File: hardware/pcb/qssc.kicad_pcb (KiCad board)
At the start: 6 copper layers, 210 x 140 mm, 126 parts, among them J1 FT232RL, J10 USB-C, J12 BTB_HOST, J2 5V Barrel, J3 SMA, J4 12V LED, J7 RESET, J8 MW_GATE, J9 JTAG, U1 XC7A35T-1CSG324C, U3 ADF4351BCPZ, U5 GVA-84+, U8 W25Q128JVSIQ, Y1 100MHz TCXO

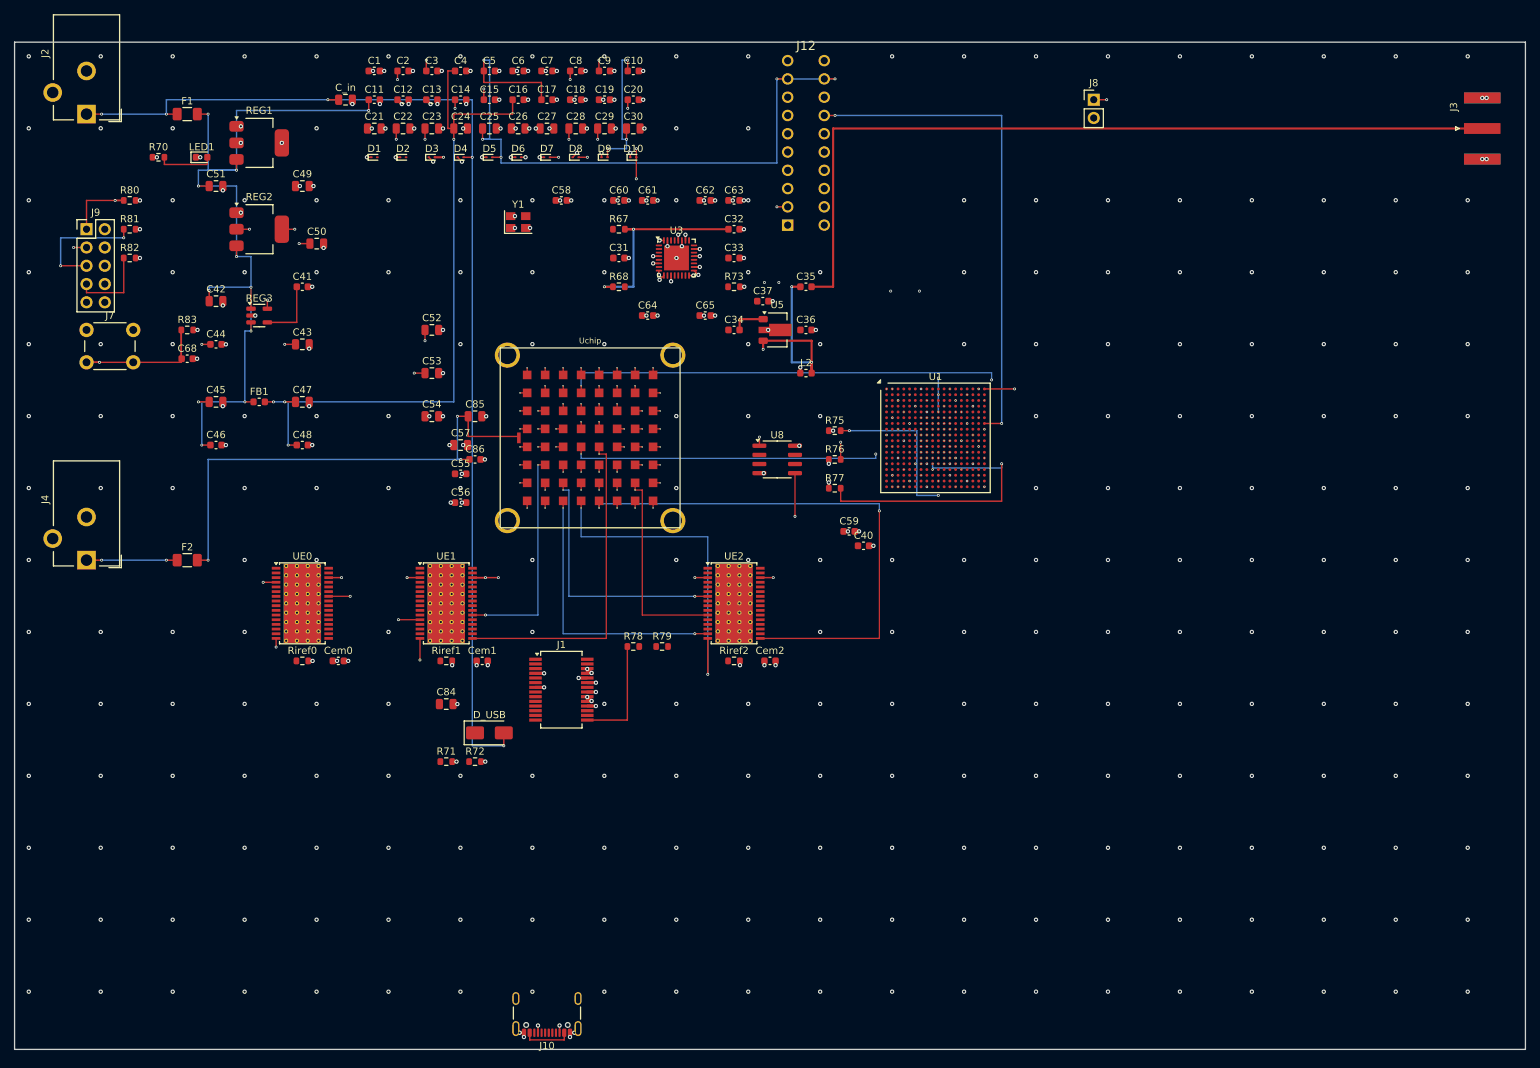
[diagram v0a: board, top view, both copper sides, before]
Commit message: head: bump detector head to 6 layers (4 signal layers for the die bus)
The 4-layer head put the 64-net die bus (DET_IN + DET_TIA) on only 2 signal
layers (F.Cu/B.Cu), at the autorouter's density ceiling.  6 layers add
In3.Cu + In4.Cu signal layers so route_signals + FreeRouting have 4 signal
layers (F.Cu/In3.Cu/In4.Cu/B.Cu).  route_signals.build() auto-selects the
4-signal-layer set from GetCopperLayerCount() (>4 branch), no router edit
needed; route_qssc_pcb reads plane labels dynamically.  HEAD_STACK_UP is a
6-layer 1.6mm FR4 build (In1.Cu GND one 0.15mm prepreg below F.Cu for the
TIA->ADC analog reference).  Die Uchip 64 DET pads stay on B.Cu.

Main board (qssc.*) is regenerated too: the JTAG J9 pin-9 +3V3 (VREF) fix
now comes from the generator code (replacing the earlier surgical edit),
and the .kicad_pcb is re-serialised in generator format (cosmetic
normalisation -- no layout/net change).  ruff CI rule clean.

Co-Authored-By: Claude Code <noreply@anthropic.com>
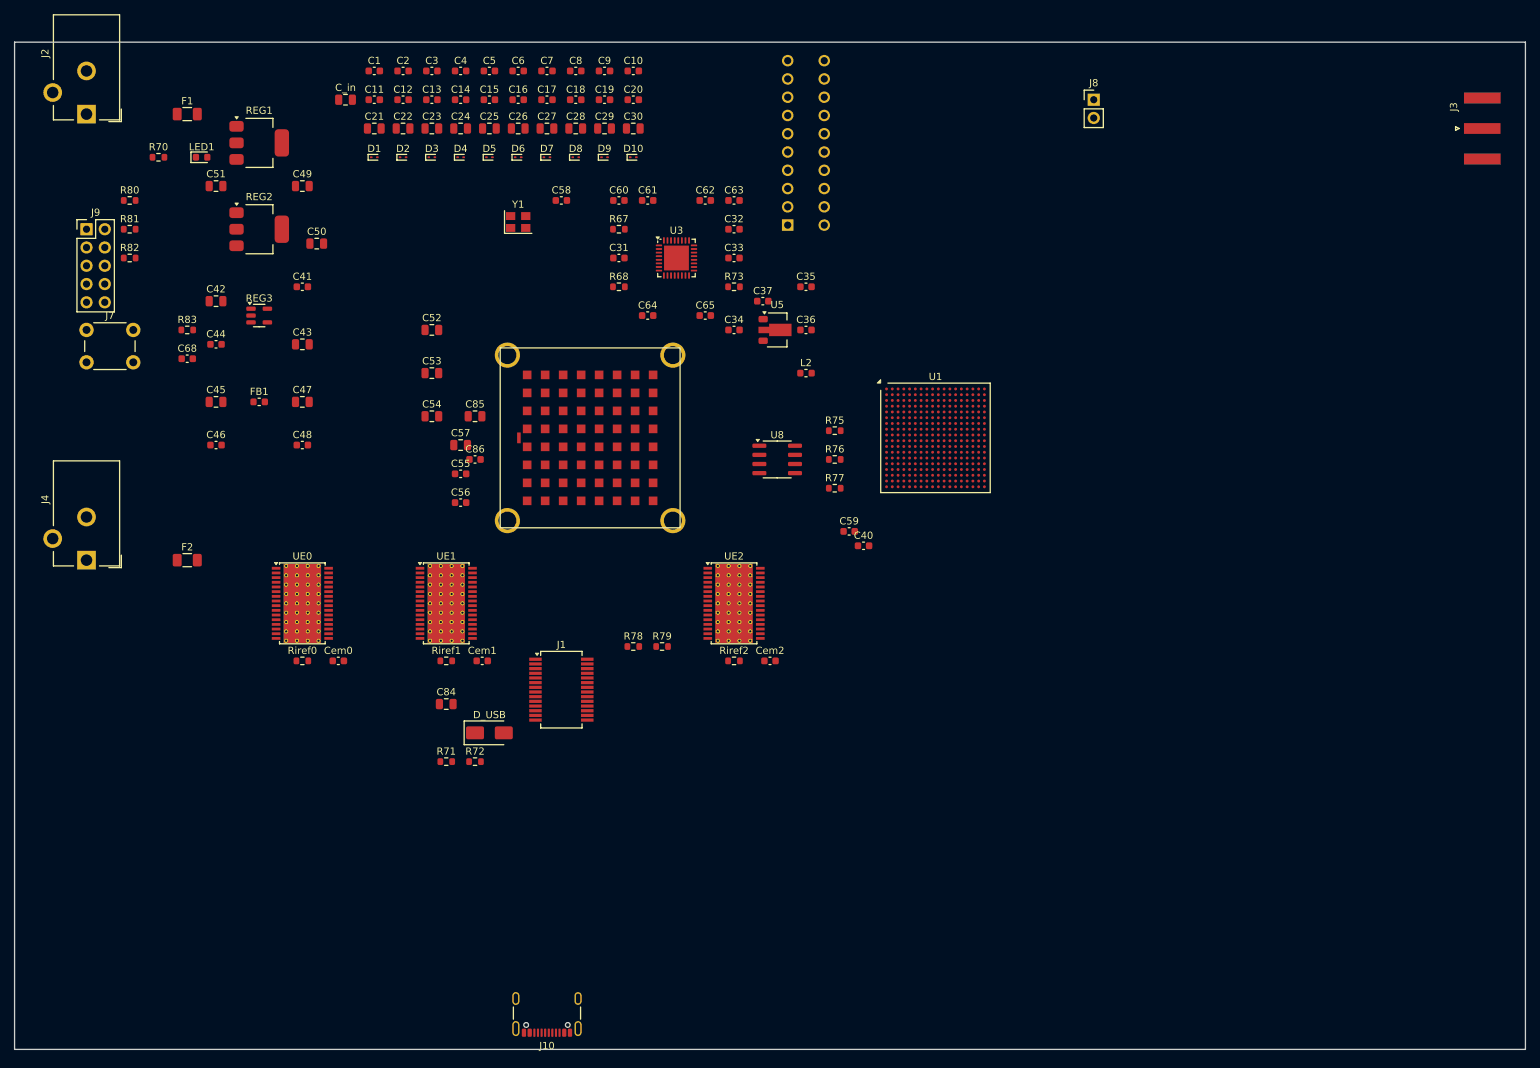
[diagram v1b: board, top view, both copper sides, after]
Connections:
- U3 pad : (no net) -> GND
- UE0 pad : (no net) -> GND
- UE1 pad : (no net) -> GND
- UE2 pad : (no net) -> GND
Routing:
- net +1V0: track 255.6 -> 0.00 mm, vias 27 -> 0
- net +5V: track 216.3 -> 0.00 mm, vias 16 -> 0
- net emitter_cat11: track 198.6 -> 0.00 mm, vias 3 -> 0
- net +1V8: track 157.6 -> 0.00 mm, vias 16 -> 0
- net +5V_IN: track 155.8 -> 0.00 mm, vias 5 -> 0
- net TCK: track 154.6 -> 0.00 mm, vias 3 -> 0
- net mw_gate: track 151.8 -> 0.00 mm, vias 5 -> 0
- net emitter_cat35: track 147.7 -> 0.00 mm, vias 3 -> 0
- net TDO: track 147.3 -> 0.00 mm, vias 2 -> 0
- net reset: track 138.6 -> 0.00 mm, vias 2 -> 0
- net em_xlat: track 137.1 -> 0.00 mm, vias 5 -> 0
- net em_sclk: track 122.2 -> 0.00 mm, vias 2 -> 0
- net +5V_RF: track 116.7 -> 0.00 mm, vias 8 -> 0
- net J3_SIG: track 115.2 -> 0.00 mm
- net em_sin: track 102.5 -> 0.00 mm, vias 2 -> 0
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- removed copper zone on In2.Cu, net +3V3
- removed copper zone on In1.Cu, net GND

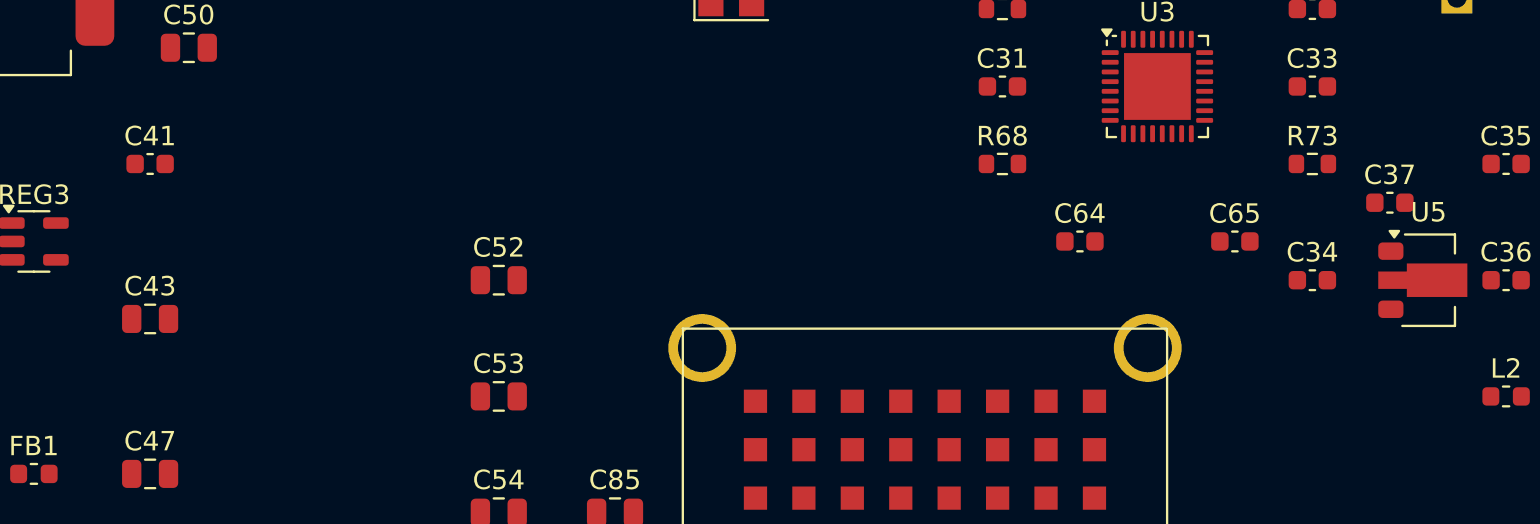
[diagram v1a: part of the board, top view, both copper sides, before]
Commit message: pins: per-datasheet fixes (ADF4351 VCOM, FT232 CBUS0/NC, AP2127K pin4) + FPGA clock on P-side MRCC
Per-datasheet verification of all 11 components (real PDFs / KiCad symbols /
manufacturer datasheets) found 4 confirmed pin defects, now fixed:

- ADF4351 pin 23 (VCOM, internal compensation node biased at half the tuning
  range) was tied direct to GND -- shorting the half-range bias. Now decoupled
  to GND via a 100nF cap on a dedicated ADF_VCOM net (mirrors VREF/C36 and
  TEMP/C37). Verified from ADF4351.pdf p8 Pin Function table.
- FT232RL pin 23 is CBUS0 (not AGND); pin 24 is NC (not a 2nd VCC pad). The
  prior 'fix' tied 23->GND and 24->+3V3 under a wrong pin belief. Now both are
  no_connect; the real AGND is pin 25 (already GND). TXD/RXD comment labels
  corrected (nets are named from the FPGA side); 3V3OUT decoupler is C55 not C57.
  Verified from the KiCad Interface_USB:FT232RL symbol (omits NC pads 8 & 24).
- AP2127K-1.0 (REG3) fixed-output pin 4 is NC, not BP -- the prior C41 10nF
  tied a cap to a floating NC pad. Pin 4 -> no_connect; C41 designator reused
  for the ADF4351 VCOM decoupling cap. Noise reduction is via CIN/COUT
  (C42/C43/C44). Verified from Diodes AP2127K DS36478.
- FPGA clk_100mhz was on the N-side MRCC (A8), forcing a CLOCK_DEDICATED_ROUTE
  FALSE workaround (fabric routing, higher jitter). gen_fpga_ballmap_csg324.py
  now puts the input clock on the P-side MRCC (B8, dedicated delay-compensated
  route) and refclk_out on the N-side (A8); the XDC workaround is removed.
  Per UG472. Stale 'A14' doc references for refclk_25m corrected.

Label: the Abracon ASE 100 MHz oscillator is an XO (not a TCXO); schematic/BOM
value and comments corrected. Boards regenerated (both boards pick up the
ballmap swap + shared symbol-lib changes). HARDWARE_DESIGN.md pin-audit table
rows for FT232RL and ADF4351 corrected.

Co-Authored-By: Claude Code <noreply@anthropic.com>
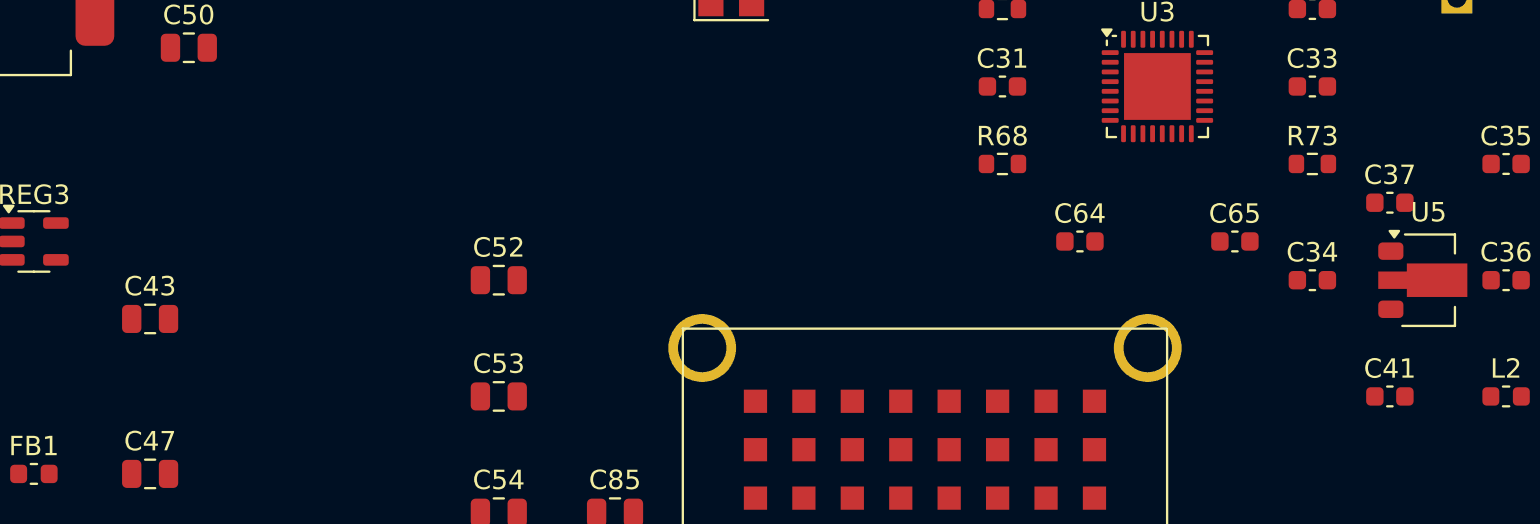
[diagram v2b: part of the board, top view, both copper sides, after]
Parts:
- C41: value 10nF -> 100n
- Y1: value 100MHz TCXO -> 100MHz XO
- moved C41 65.1 mm to (104.0, 46.0)
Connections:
- C41 pad 1: BP_1V0 -> ADF_VCOM
- J1 pad 23: GND -> (no net)
- J1 pad 24: +3V3 -> (no net)
- REG3 pad 4: BP_1V0 -> (no net)
- U1 pad A8: clk_100mhz -> refclk_25m
- U1 pad B8: refclk_25m -> clk_100mhz
- U3 pad 23: GND -> ADF_VCOM
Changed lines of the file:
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@@
 	(net 10 "ADF_MUXOUT")
 	(net 11 "ADF_TEMP")
-	(net 12 "BP_1V0")
+	(net 12 "ADF_VCOM")
 	(net 13 "CC1")
 	(net 14 "CC2")
@@
 			(size 1.325 0.6)
 			(layers "F.Cu" "F.Paste" "F.Mask")
-			(net 12 "BP_1V0")
 			(roundrect_rratio 0.25)
 		)
@@
 		)
 	)
-	(footprint "C_0603_1608Metric"
-		(version 20240108)
-		(generator "pcbnew")
-		(generator_version "8.0")
-		(layer "F.Cu")
-		(at 40 34 0)
-		(descr "Capacitor SMD 0603 (1608 Metric), square (rectangular) end terminal, IPC_7351 nominal, (Body size source: IPC-SM-782 page 76, https://www.pcb-3d.com/wordpress/wp-content/uploads/ipc-sm-782a_amendment_1_and_2.pdf), generated with kicad-footprint-generator")
-		(tags "capacitor")
-		(property "Reference" "C41"
-			(at 0 -1.43 0)
-			(layer "F.SilkS")
-			(effects
-				(font
-					(size 1 1)
-					(thickness 0.15)
-				)
-			)
-		)
-		(property "Value" "10nF"
-			(at 0 1.43 0)
-			(layer "F.Fab")
-			(effects
-				(font
-					(size 1 1)
-					(thickness 0.15)
-				)
-			)
-		)
-		(property "Footprint" ""
-			(at 0 0 0)
-			(unlocked yes)
-			(layer "F.Fab")
-			(hide yes)
-			(effects
-				(font
-					(size 1.27 1.27)
-				)
-			)
-		)
-		(property "Datasheet" ""
-			(at 0 0 0)
-			(unlocked yes)
-			(layer "F.Fab")
-			(hide yes)
-			(effects
-				(font
-					(size 1.27 1.27)
-				)
-			)
-		)
-		(property "Description" ""
-			(at 0 0 0)
-			(unlocked yes)
-			(layer "F.Fab")
-			(hide yes)
-			(effects
-				(font
-					(size 1.27 1.27)
-				)
-			)
-		)
-		(attr smd)
-		(fp_line
-			(start -0.14058 -0.51)
-			(end 0.14058 -0.51)
-			(stroke
-				(width 0.12)
-				(type solid)
-			)
-			(layer "F.SilkS")
-		)
-		(fp_line
-			(start -0.14058 0.51)
-			(end 0.14058 0.51)
-			(stroke
-				(width 0.12)
-				(type solid)
-			)
-			(layer "F.SilkS")
-		)
-		(fp_line
-			(start -1.48 -0.73)
-			(end 1.48 -0.73)
-			(stroke
-				(width 0.05)
-				(type solid)
-			)
-			(layer "F.CrtYd")
-		)
-		(fp_line
-			(start -1.48 0.73)
-			(end -1.48 -0.73)
-			(stroke
-				(width 0.05)
-				(type solid)
-			)
-			(layer "F.CrtYd")
-		)
-		(fp_line
-			(start 1.48 -0.73)
-			(end 1.48 0.73)
-			(stroke
-				(width 0.05)
-				(type solid)
-			)
-			(layer "F.CrtYd")
-		)
-		(fp_line
-			(start 1.48 0.73)
-			(end -1.48 0.73)
-			(stroke
-				(width 0.05)
-				(type solid)
-			)
-			(layer "F.CrtYd")
-		)
-		(fp_line
-			(start -0.8 -0.4)
-			(end 0.8 -0.4)
-			(stroke
-				(width 0.1)
-				(type solid)
-			)
-			(layer "F.Fab")
-		)
-		(fp_line
-			(start -0.8 0.4)
-			(end -0.8 -0.4)
-			(stroke
-				(width 0.1)
-				(type solid)
-			)
-			(layer "F.Fab")
-		)
-		(fp_line
-			(start 0.8 -0.4)
-			(end 0.8 0.4)
-			(stroke
-				(width 0.1)
-				(type solid)
-			)
-			(layer "F.Fab")
-		)
-		(fp_line
-			(start 0.8 0.4)
-			(end -0.8 0.4)
-			(stroke
-				(width 0.1)
-				(type solid)
-			)
-			(layer "F.Fab")
-		)
-		(fp_text user "${REFERENCE}"
-			(at 0 0 0)
-			(layer "F.Fab")
-			(effects
-				(font
-					(size 0.4 0.4)
-					(thickness 0.06)
-				)
-			)
-		)
-		(pad "1" smd roundrect
-			(at -0.775 0)
-			(size 0.9 0.95)
-			(layers "F.Cu" "F.Paste" "F.Mask")
-			(net 12 "BP_1V0")
-			(roundrect_rratio 0.25)
-		)
-		(pad "2" smd roundrect
-			(at 0.775 0)
-			(size 0.9 0.95)
-			(layers "F.Cu" "F.Paste" "F.Mask")
-			(net 18 "GND")
-			(roundrect_rratio 0.25)
-		)
-		(model "${KICAD8_3DMODEL_DIR}/Capacitor_SMD.3dshapes/C_0603_1608Metric.wrl"
-			(offset
-				(xyz 0 0 0)
-			)
-			(scale
-				(xyz 1 1 1)
-			)
-			(rotate
-				(xyz 0 0 0)
-			)
-		)
-	)
 	(footprint "C_0805_2012Metric"
 		(version 20240108)
@@
 			(property pad_prop_bga)
 			(layers "F.Cu" "F.Paste" "F.Mask")
-			(net 59 "clk_100mhz")
+			(net 135 "refclk_25m")
 		)
 		(pad "A9" smd circle
@@
 			(property pad_prop_bga)
 			(layers "F.Cu" "F.Paste" "F.Mask")
-			(net 135 "refclk_25m")
+			(net 59 "clk_100mhz")
 		)
 		(pad "B9" smd circle
@@
 			)
 		)
-		(property "Value" "100MHz TCXO"
+		(property "Value" "100MHz XO"
 			(at 0 2.45 0)
 			(layer "F.Fab")
@@
 			(size 1.75 0.45)
 			(layers "F.Cu" "F.Paste" "F.Mask")
-			(net 18 "GND")
 		)
 		(pad "24" smd rect
@@
 			(size 1.75 0.45)
 			(layers "F.Cu" "F.Paste" "F.Mask")
-			(net 5 "+3V3")
 		)
 		(pad "25" smd rect
@@
 			(size 0.875 0.25)
 			(layers "F.Cu" "F.Paste" "F.Mask")
-			(net 18 "GND")
+			(net 12 "ADF_VCOM")
 			(roundrect_rratio 0.25)
 		)
@@
 			(roundrect_rratio 0.25)
 		)
+		(pad "2" smd roundrect
+			(at 0.775 0)
+			(size 0.9 0.95)
+			(layers "F.Cu" "F.Paste" "F.Mask")
+			(net 18 "GND")
+			(roundrect_rratio 0.25)
+		)
+		(model "${KICAD8_3DMODEL_DIR}/Capacitor_SMD.3dshapes/C_0603_1608Metric.wrl"
+			(offset
+				(xyz 0 0 0)
+			)
+			(scale
+				(xyz 1 1 1)
+			)
+			(rotate
+				(xyz 0 0 0)
+			)
+		)
+	)
+	(footprint "C_0603_1608Metric"
+		(version 20240108)
+		(generator "pcbnew")
+		(generator_version "8.0")
+		(layer "F.Cu")
+		(at 104 46 0)
+		(descr "Capacitor SMD 0603 (1608 Metric), square (rectangular) end terminal, IPC_7351 nominal, (Body size source: IPC-SM-782 page 76, https://www.pcb-3d.com/wordpress/wp-content/uploads/ipc-sm-782a_amendment_1_and_2.pdf), generated with kicad-footprint-generator")
+		(tags "capacitor")
+		(property "Reference" "C41"
+			(at 0 -1.43 0)
+			(layer "F.SilkS")
+			(effects
+				(font
+					(size 1 1)
+					(thickness 0.15)
+				)
+			)
+		)
+		(property "Value" "100n"
+			(at 0 1.43 0)
+			(layer "F.Fab")
+			(effects
+				(font
+					(size 1 1)
+					(thickness 0.15)
+				)
+			)
+		)
+		(property "Footprint" ""
+			(at 0 0 0)
+			(unlocked yes)
+			(layer "F.Fab")
+			(hide yes)
+			(effects
+				(font
+					(size 1.27 1.27)
+				)
+			)
+		)
+		(property "Datasheet" ""
+			(at 0 0 0)
+			(unlocked yes)
+			(layer "F.Fab")
+			(hide yes)
+			(effects
+				(font
+					(size 1.27 1.27)
+				)
+			)
+		)
+		(property "Description" ""
+			(at 0 0 0)
+			(unlocked yes)
+			(layer "F.Fab")
+			(hide yes)
+			(effects
+				(font
+					(size 1.27 1.27)
+				)
+			)
+		)
+		(attr smd)
+		(fp_line
+			(start -0.14058 -0.51)
+			(end 0.14058 -0.51)
+			(stroke
+				(width 0.12)
+				(type solid)
+			)
+			(layer "F.SilkS")
+		)
+		(fp_line
+			(start -0.14058 0.51)
+			(end 0.14058 0.51)
+			(stroke
+				(width 0.12)
+				(type solid)
+			)
+			(layer "F.SilkS")
+		)
+		(fp_line
+			(start -1.48 -0.73)
+			(end 1.48 -0.73)
+			(stroke
+				(width 0.05)
+				(type solid)
+			)
+			(layer "F.CrtYd")
+		)
+		(fp_line
+			(start -1.48 0.73)
+			(end -1.48 -0.73)
+			(stroke
+				(width 0.05)
+				(type solid)
+			)
+			(layer "F.CrtYd")
+		)
+		(fp_line
+			(start 1.48 -0.73)
+			(end 1.48 0.73)
+			(stroke
+				(width 0.05)
+				(type solid)
+			)
+			(layer "F.CrtYd")
+		)
+		(fp_line
+			(start 1.48 0.73)
+			(end -1.48 0.73)
+			(stroke
+				(width 0.05)
+				(type solid)
+			)
+			(layer "F.CrtYd")
+		)
+		(fp_line
+			(start -0.8 -0.4)
+			(end 0.8 -0.4)
+			(stroke
+				(width 0.1)
+				(type solid)
+			)
+			(layer "F.Fab")
+		)
+		(fp_line
+			(start -0.8 0.4)
+			(end -0.8 -0.4)
+			(stroke
+				(width 0.1)
+				(type solid)
+			)
+			(layer "F.Fab")
+		)
+		(fp_line
+			(start 0.8 -0.4)
+			(end 0.8 0.4)
+			(stroke
+				(width 0.1)
+				(type solid)
+			)
+			(layer "F.Fab")
+		)
+		(fp_line
+			(start 0.8 0.4)
+			(end -0.8 0.4)
+			(stroke
+				(width 0.1)
+				(type solid)
+			)
+			(layer "F.Fab")
+		)
+		(fp_text user "${REFERENCE}"
+			(at 0 0 0)
+			(layer "F.Fab")
+			(effects
+				(font
+					(size 0.4 0.4)
+					(thickness 0.06)
+				)
+			)
+		)
+		(pad "1" smd roundrect
+			(at -0.775 0)
+			(size 0.9 0.95)
+			(layers "F.Cu" "F.Paste" "F.Mask")
+			(net 12 "ADF_VCOM")
+			(roundrect_rratio 0.25)
+		)
